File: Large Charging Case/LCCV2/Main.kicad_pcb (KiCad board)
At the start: 2 copper layers, 139.9 x 57.8 mm, 238 parts, among them J1 Conn_02x05_Odd_Even, J10 Coil A, J11 Coil B, J12 TX_Coil, J13 Coil A, J14 Coil B, J15 TX_Coil, J16 Coil A, J17 Coil B, J18 TX_Coil, J19 Coil A, J2 Coil B, J20 Coil B, J21 TX_Coil, J22 Coil A, J23 USB_C_Receptacle_USB2.0, J24 Conn_01x02, J25 Coil B, J26 TX_Coil, J27 Coil A, J3 TX_Coil, J4 Coil A, J5 Coil B, J6 TX_Coil, J7 Coil A, J8 Coil B, J9 TX_Coil, SW1 SW_Push, U1 N52810_QFN32, U10 XKT001, U11 XKT335, U12 XKT001, U13 XKT335, U14 XKT001, U15 XKT335, U16 INA4180A4, U17 DG4051E, U18 INA4180A4, U19 74HCT259, U2 XKT001, U20 BQ24232H, U21 XL6007E1, U22 LN3406, U23 XKT001, U24 XKT335, U3 XKT335, U4 XKT001, U5 XKT335, U6 XKT001, U7 XKT335, U8 XKT001, U9 XKT335, Y1 32MHz 40ppm

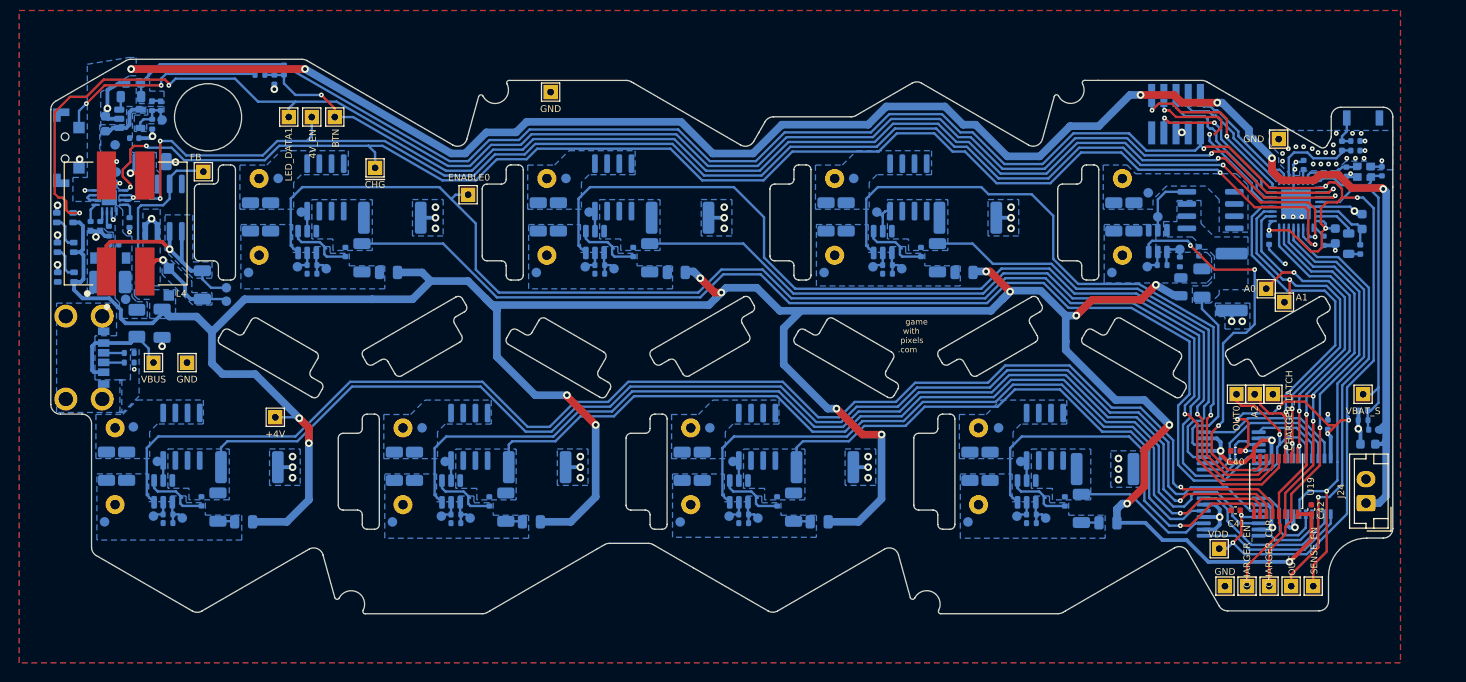
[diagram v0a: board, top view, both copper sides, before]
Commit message: Updating D8 and D10 boards, new antenna, etc...
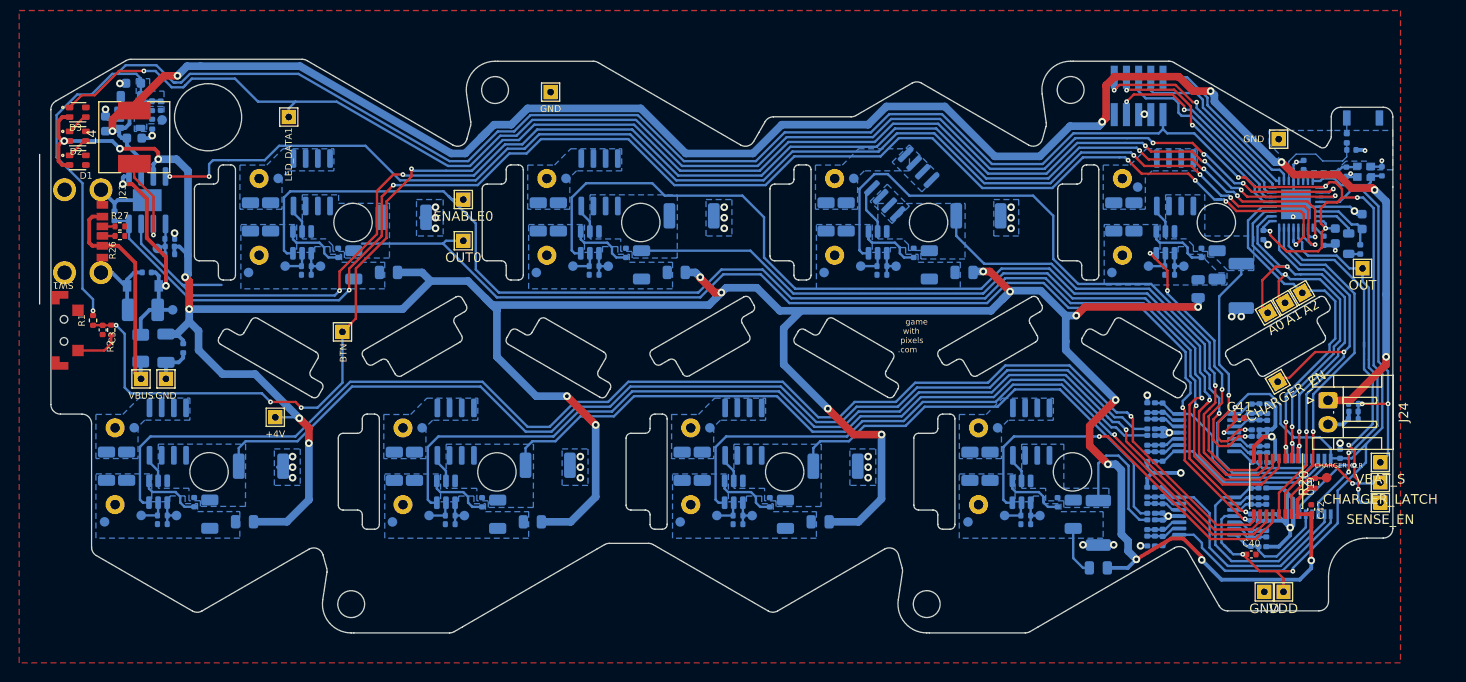
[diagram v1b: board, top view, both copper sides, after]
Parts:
- removed C9: DNP, Capacitor_SMD:C_0402_1005Metric
- removed D4: 30V 2A, Diode_SMD:D_SOD-123F
- removed U21: XL6007E1, Pixels-dice:SOIC-8_3.9x4.9mm_P1.27mm
- removed W11, W16, W21, W26, W31, W36, W6, W73: G, Pixels-dice:TEST_PIN
- removed W60: ~{PGOOD}, Pixels-dice:TEST_PIN
- removed W63: VDC, Pixels-dice:TEST_PIN
- removed W64: SWC, Pixels-dice:TEST_PIN
- removed W66: SW, Pixels-dice:TEST_PIN
- removed W78: ~{CHG}, Pixels-dice:TestPoint_THTPad_1.5x1.5mm_Drill0.7mm
- removed W79: 4V_EN, Pixels-dice:TestPoint_THTPad_1.5x1.5mm_Drill0.7mm
- added C59: 0.1uF 10V 20%, Capacitor_SMD:C_0402_1005Metric, B.Cu at (181.4, 109.3)
- added C60: 0.1uF 10V 20%, Capacitor_SMD:C_0402_1005Metric, B.Cu at (182.2, 111.0)
- added C61: 0.1uF 10V 20%, Capacitor_SMD:C_0402_1005Metric, B.Cu at (172.2, 114.3)
- added C62: 0.1uF 10V 20%, Capacitor_SMD:C_0402_1005Metric, B.Cu at (172.2, 112.6)
- added C63: 0.1uF 10V 20%, Capacitor_SMD:C_0402_1005Metric, B.Cu at (172.2, 109.2)
- added C64: 0.1uF 10V 20%, Capacitor_SMD:C_0402_1005Metric, B.Cu at (172.2, 110.9)
- added C65: 0.1uF 10V 20%, Capacitor_SMD:C_0402_1005Metric, B.Cu at (181.5, 100.5)
- added C66: 0.1uF 10V 20%, Capacitor_SMD:C_0402_1005Metric, B.Cu at (183.1, 102.2)
- added C67: 0.1uF 10V 20%, Capacitor_SMD:C_0402_1005Metric, B.Cu at (181.5, 105.6)
- added C68: 0.1uF 10V 20%, Capacitor_SMD:C_0402_1005Metric, B.Cu at (183.1, 103.9)
- added C69: 0.1uF 10V 20%, Capacitor_SMD:C_0402_1005Metric, B.Cu at (172.2, 105.5)
- added C70: 0.1uF 10V 20%, Capacitor_SMD:C_0402_1005Metric, B.Cu at (172.2, 103.8)
- added C71: 0.1uF 10V 20%, Capacitor_SMD:C_0402_1005Metric, B.Cu at (172.2, 100.4)
- added C72: 0.1uF 10V 20%, Capacitor_SMD:C_0402_1005Metric, B.Cu at (172.2, 102.1)
- added R39: 100k 0.1%, Resistor_SMD:R_0402_1005Metric, B.Cu at (171.4, 114.3)
- added R40: 2k 0.1%, Resistor_SMD:R_0402_1005Metric, B.Cu at (170.6, 114.3)
- added R41: 100mR 0.5W 1%, Resistor_SMD:R_2010_5025Metric, B.Cu at (165.5, 112.4)
- added R42: 2k 0.1%, Resistor_SMD:R_0402_1005Metric, B.Cu at (170.6, 112.6)
- added R43: 100k 0.1%, Resistor_SMD:R_0402_1005Metric, B.Cu at (171.4, 112.6)
- added R44: 100k 0.1%, Resistor_SMD:R_0402_1005Metric, B.Cu at (171.4, 109.2)
- added R45: 2k 0.1%, Resistor_SMD:R_0402_1005Metric, B.Cu at (170.6, 109.2)
- added R46: 100mR 0.5W 1%, Resistor_SMD:R_2010_5025Metric, B.Cu at (138.1, 106.5)
- added R47: 2k 0.1%, Resistor_SMD:R_0402_1005Metric, B.Cu at (170.6, 110.9)
- added R48: 100k 0.1%, Resistor_SMD:R_0402_1005Metric, B.Cu at (171.4, 110.9)
- added R49: 100k 0.1%, Resistor_SMD:R_0402_1005Metric, B.Cu at (182.3, 100.5)
- added R50: 2k 0.1%, Resistor_SMD:R_0402_1005Metric, B.Cu at (183.1, 100.5)
- added R51: 100mR 0.5W 1%, Resistor_SMD:R_2010_5025Metric, B.Cu at (180.4, 87.7)
- added R52: 2k 0.1%, Resistor_SMD:R_0402_1005Metric, B.Cu at (181.5, 102.2)
- added R53: 100k 0.1%, Resistor_SMD:R_0402_1005Metric, B.Cu at (182.3, 102.2)
- added R54: 100k 0.1%, Resistor_SMD:R_0402_1005Metric, B.Cu at (182.3, 105.6)
- added R55: 2k 0.1%, Resistor_SMD:R_0402_1005Metric, B.Cu at (183.1, 105.6)
- added R56: 100mR 0.5W 1%, Resistor_SMD:R_2010_5025Metric, B.Cu at (153.0, 80.4)
- added R57: 2k 0.1%, Resistor_SMD:R_0402_1005Metric, B.Cu at (181.5, 103.9)
- added R58: 100k 0.1%, Resistor_SMD:R_0402_1005Metric, B.Cu at (182.3, 103.9)
- added R59: 100k 0.1%, Resistor_SMD:R_0402_1005Metric, B.Cu at (171.4, 105.5)
- added R60: 2k 0.1%, Resistor_SMD:R_0402_1005Metric, B.Cu at (170.6, 105.5)
- added R61: 100mR 0.5W 1%, Resistor_SMD:R_2010_5025Metric, B.Cu at (108.1, 106.4)
- added R62: 2k 0.1%, Resistor_SMD:R_0402_1005Metric, B.Cu at (170.6, 103.8)
- added R63: 100k 0.1%, Resistor_SMD:R_0402_1005Metric, B.Cu at (171.4, 103.8)
- added R64: 100k 0.1%, Resistor_SMD:R_0402_1005Metric, B.Cu at (171.4, 100.4)
- added R65: 2k 0.1%, Resistor_SMD:R_0402_1005Metric, B.Cu at (170.6, 100.4)
- added R66: 100mR 0.5W 1%, Resistor_SMD:R_2010_5025Metric, B.Cu at (78.2, 106.5)
- added R67: 2k 0.1%, Resistor_SMD:R_0402_1005Metric, B.Cu at (170.6, 102.1)
- added R68: 100k 0.1%, Resistor_SMD:R_0402_1005Metric, B.Cu at (171.4, 102.1)
- C3, D1, D2, D3, J23, R1, R2, R26, R27, SW1: moved to F.Cu
- C45: value 0.1uF 10V 20% -> 4.7uF 6.3V 20%; footprint Capacitor_SMD:C_0402_1005Metric -> Capacitor_SMD:C_0603_1608Metric
- C46: value 47uF 10V 20% -> 22pF 10V 5%; footprint Capacitor_SMD:C_1206_3216Metric -> Capacitor_SMD:C_0402_1005Metric
- C49: value 4.7uF 6.3V 20% -> 0.1uF 10V 20%; footprint Capacitor_SMD:C_0603_1608Metric -> Capacitor_SMD:C_0402_1005Metric
- C5, C6: value 6pF 10V 10% -> 8pF 10V 10%
- C50: value 47uF 10V 20% -> 0.1uF 10V 20%; footprint Capacitor_SMD:C_1206_3216Metric -> Capacitor_SMD:C_0402_1005Metric
- C8: value 1.5pF 10V NP0 -> 0.8pF 10V NP0
- J24: footprint Connector_JST:JST_EH_B2B-EH-A_1x02_P2.50mm_Vertical -> Connector_JST:JST_EH_S2B-EH_1x02_P2.50mm_Horizontal
- L4: value 22uH 2A 20% -> 4.7uH 1.5A 10%; footprint Pixels-dice:Murata 4700 -> Pixels-dice:SPM6530
- R17: value 30mR 2W 1% -> 470k 1%; footprint Resistor_SMD:R_2512_6332Metric -> Resistor_SMD:R_0402_1005Metric
- R18: value 30mR 2W 1% -> 1k 1%; footprint Resistor_SMD:R_2512_6332Metric -> Resistor_SMD:R_0402_1005Metric
- R19: value 30mR 2W 1% -> 100k 1%; footprint Resistor_SMD:R_2512_6332Metric -> Resistor_SMD:R_0402_1005Metric
- R20: value 30mR 2W 1% -> 100k 1%; footprint Resistor_SMD:R_2512_6332Metric -> Resistor_SMD:R_0402_1005Metric; moved to F.Cu
- R21: value 30mR 2W 1% -> 100k 0.1%; footprint Resistor_SMD:R_2512_6332Metric -> Resistor_SMD:R_0402_1005Metric
- R22, R24: value 30mR 2W 1% -> 2k 0.1%; footprint Resistor_SMD:R_2512_6332Metric -> Resistor_SMD:R_0402_1005Metric
- R23: value 30mR 2W 1% -> 100mR 0.5W 1%; footprint Resistor_SMD:R_2512_6332Metric -> Resistor_SMD:R_2010_5025Metric
- R25: value 8.66k 1% -> 100k 0.1%
- R28: value 10k 5% -> 100k 0.1%
- R29: value 3k 1% -> 2k 0.1%
- R30: value 1k 1% -> 100mR 0.5W 1%; footprint Resistor_SMD:R_0402_1005Metric -> Resistor_SMD:R_2010_5025Metric
- R31: value 1.8k 1% -> 2k 0.1%
- R32: value 3.32k 1% -> 100k 0.1%
- U16: value INA4180A4 -> LP78071; footprint Package_SO:TSSOP-14_4.4x5mm_P0.65mm -> Pixels-dice:SOIC-8-1EP_3.9x4.9mm_P1.27mm_EP2.29x3mm
- U17: value DG4051E -> 74HC4051PW
- U18: value INA4180A4 -> LM2902
- U20: value BQ24232H -> LM2902; footprint Package_DFN_QFN:VQFN-16-1EP_3x3mm_P0.5mm_EP1.6x1.6mm -> Package_SO:TSSOP-14_4.4x5mm_P0.65mm
- W59: footprint Pixels-dice:TestPoint_THTPad_1.5x1.5mm_Drill0.7mm -> Pixels-dice:TEST_PIN
- W67: footprint Pixels-dice:TestPoint_THTPad_1.5x1.5mm_Drill0.7mm -> Pixels-dice:TEST_PIN; moved to B.Cu
- moved R28 124.9 mm to (182.2, 109.3)
- moved R29 123.7 mm to (183.0, 109.3)
- moved R31 123.5 mm to (181.4, 111.0), turned to 90 degrees
- moved R25 120.2 mm to (183.0, 112.7), turned to -90 degrees
- moved R32 119.6 mm to (183.0, 111.0), turned to 90 degrees
- moved U20 117.0 mm to (176.8, 103.0), turned to 180 degrees
- moved U16 116.0 mm to (66.3, 78.8), turned to 90 degrees
- moved C50 112.9 mm to (182.2, 112.7), turned to 90 degrees
- moved R24 104.6 mm to (181.4, 112.7), turned to -90 degrees
- moved R19 83.2 mm to (68.7, 82.8)
- moved W40 82.2 mm to (99.3, 83.0)
- moved R18 59.0 mm to (62.9, 80.4), turned to 90 degrees
- moved R30 58.6 mm to (123.1, 80.4), turned to 180 degrees
- moved R22 46.7 mm to (183.0, 114.4), turned to 90 degrees
- moved W47 33.9 mm to (193.0, 85.9)
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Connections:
- net Net-(AE1-Pad1) renamed /ANT_CHIP
- net Net-(C8-Pad2) renamed /ANT_NRF
- C45 pad 1: +VDC -> +BATT
- C46 pad 1: +VDC -> +4V
- C46 pad 2: GND -> Net-(C46-Pad2)
- C49 pad 1: +BATT -> Net-(C49-Pad1)
- C49 pad 2: GND -> /Multiplexed Chargers/SENSE5
- C50 pad 2: Net-(C50-Pad2) -> GND
- C53 pad 1: +VDC -> +BATT
- L4 pad 1: Net-(C50-Pad1) -> Net-(L4-Pad1)
- L4 pad 2: Net-(C50-Pad2) -> +BATT
- R17 pad 1: GND -> Net-(C46-Pad2)
- R17 pad 2: /Multiplexed Chargers/Charger 1/CHARGER_GND -> +4V
- R18 pad 1: GND -> /Power/BAT_I_SENSE
- R18 pad 2: /Multiplexed Chargers/Charger 2/CHARGER_GND -> GND
- R19 pad 2: /Multiplexed Chargers/Charger 3/CHARGER_GND -> Net-(C46-Pad2)
- R20 pad 1: GND -> +4V
- R20 pad 2: /Multiplexed Chargers/Charger 4/CHARGER_GND -> Net-(R20-Pad2)
- R21 pad 1: GND -> /Multiplexed Chargers/SENSE5
- R21 pad 2: /Multiplexed Chargers/Charger 5/CHARGER_GND -> Net-(C49-Pad1)
- R22 pad 2: /Multiplexed Chargers/Charger 6/CHARGER_GND -> Net-(C49-Pad1)
- R23 pad 2: /Multiplexed Chargers/Charger 7/CHARGER_GND -> /Multiplexed Chargers/Charger 1/CHARGER_GND
- R24 pad 1: GND -> /Multiplexed Chargers/Charger 1/CHARGER_GND
- R24 pad 2: /Multiplexed Chargers/Charger 8/CHARGER_GND -> Net-(C50-Pad1)
- R25 pad 1: +4V -> GND
- R25 pad 2: Net-(R25-Pad2) -> Net-(C50-Pad1)
- R28 pad 1: Net-(R28-Pad1) -> /Multiplexed Chargers/SENSE7
- R28 pad 2: GND -> Net-(C59-Pad1)
- R29 pad 1: Net-(R29-Pad1) -> GND
- R29 pad 2: GND -> Net-(C59-Pad1)
- R30 pad 1: Net-(R30-Pad1) -> GND
- R30 pad 2: GND -> /Multiplexed Chargers/Charger 2/CHARGER_GND
- R31 pad 1: Net-(R31-Pad1) -> /Multiplexed Chargers/Charger 2/CHARGER_GND
- R31 pad 2: GND -> Net-(C60-Pad1)
- R32 pad 1: Net-(R25-Pad2) -> GND
- R32 pad 2: GND -> Net-(C60-Pad1)
- U1 pad 2: /Power/4V_EN -> /Power/CHARGE
- U1 pad 3: /Power/~{CHG} -> /Power/4V_EN
- U1 pad 5: /Multiplexed Chargers/SENSE_EN -> /Power/BAT_I_SENSE
- U1 pad 6: /Multiplexed Chargers/~{CHARGER_ENL_CLR} -> /Multiplexed Chargers/SENSE_EN
- U10 pad 6: /Multiplexed Chargers/ENABLE5 -> /Multiplexed Chargers/ENABLE6
- U12 pad 6: /Multiplexed Chargers/ENABLE6 -> /Multiplexed Chargers/ENABLE5
- U14 pad 6: /Multiplexed Chargers/ENABLE7 -> /Multiplexed Chargers/ENABLE4
- U16 pad 1: /Multiplexed Chargers/SENSE0 -> Net-(C46-Pad2)
- U16 pad 2: GND -> Net-(L4-Pad1)
- U16 pad 3: /Multiplexed Chargers/Charger 2/CHARGER_GND -> /Power/CHARGE
- U16 pad 4: VDD -> /Power/BAT_I_SENSE
- U16 pad 5: /Multiplexed Chargers/Charger 1/CHARGER_GND -> +5V
- U16 pad 6: GND -> +BATT
- U16 pad 7: /Multiplexed Chargers/SENSE3 -> +4V
- U16 pad 8: /Multiplexed Chargers/SENSE1 -> /Power/4V_EN
- U18 pad 1: /Multiplexed Chargers/SENSE5 -> /Multiplexed Chargers/SENSE7
- U18 pad 10: /Multiplexed Chargers/Charger 5/CHARGER_GND -> Net-(C62-Pad1)
- U18 pad 12: /Multiplexed Chargers/Charger 6/CHARGER_GND -> Net-(C64-Pad1)
- U18 pad 13: GND -> Net-(C63-Pad1)
- U18 pad 2: GND -> Net-(C59-Pad1)
- U18 pad 3: /Multiplexed Chargers/Charger 8/CHARGER_GND -> Net-(C60-Pad1)
- U18 pad 5: /Multiplexed Chargers/Charger 7/CHARGER_GND -> Net-(C50-Pad1)
- U18 pad 6: GND -> Net-(C49-Pad1)
- U18 pad 7: /Multiplexed Chargers/SENSE7 -> /Multiplexed Chargers/SENSE5
- U18 pad 9: GND -> Net-(C61-Pad1)
- U19 pad 15: /Multiplexed Chargers/~{CHARGER_ENL_CLR} -> Net-(R20-Pad2)
- U20 pad 1: Net-(R28-Pad1) -> /Multiplexed Chargers/SENSE0
- U20 pad 10: +VDC -> Net-(C70-Pad1)
- U20 pad 11: +VDC -> GND
- U20 pad 12: Net-(R30-Pad1) -> Net-(C72-Pad1)
- U20 pad 13: +5V -> Net-(C71-Pad1)
- U20 pad 14: GND -> /Multiplexed Chargers/SENSE1
- U20 pad 2: +BATT -> Net-(C65-Pad1)
- U20 pad 3: +BATT -> Net-(C66-Pad1)
- U20 pad 4: GND -> VDD
- U20 pad 5: +VDC -> Net-(C68-Pad1)
- U20 pad 6: GND -> Net-(C67-Pad1)
- U20 pad 7: Net-(U20-Pad7) -> /Multiplexed Chargers/SENSE3
- U20 pad 8: GND -> /Multiplexed Chargers/SENSE2
- U20 pad 9: /Power/~{CHG} -> Net-(C69-Pad1)
- U22 pad 1: +VDC -> +BATT
- U22 pad 4: +VDC -> +BATT
- U23 pad 6: /Multiplexed Chargers/ENABLE4 -> /Multiplexed Chargers/ENABLE7
- W40 pad 1: /Multiplexed Chargers/SENSE3 -> /Multiplexed Chargers/Charger 1/CHARGER_GND
- W59 pad 1: /Multiplexed Chargers/~{CHARGER_ENL_CLR} -> Net-(R20-Pad2)
- W67 pad 1: Net-(R25-Pad2) -> Net-(C46-Pad2)
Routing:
- net /Power/CHARGE: track 0.00 -> 156.5 mm, vias 0 -> 6
- net /Power/BAT_I_SENSE: track 0.00 -> 154.7 mm, vias 0 -> 6
- net /Power/~{CHG}: track 150.5 -> 0.00 mm, vias 4 -> 0
- net /Multiplexed Chargers/ENABLE7: track 143.5 -> 41.1 mm
- net /Multiplexed Chargers/ENABLE4: track 40.7 -> 142.3 mm
- net /Multiplexed Chargers/~{CHARGER_ENL_CLR}: track 45.6 -> 0.00 mm, vias 1 -> 0
- net Net-(C3-Pad1): track 128.5 -> 169.2 mm, vias 3 -> 8
- net VDD: track 249.1 -> 288.5 mm, vias 12 -> 10
- net /Multiplexed Chargers/ENABLE6: track 108.9 -> 74.6 mm
- net /Multiplexed Chargers/ENABLE5: track 75.1 -> 108.0 mm
- net +4V: track 311.9 -> 342.8 mm, vias 15 -> 22
- net +5V: track 0.00 -> 25.1 mm, vias 0 -> 2
- net /Multiplexed Chargers/Charger 7/CHARGER_GND: track 97.4 -> 75.0 mm
- net /Multiplexed Chargers/Charger 8/CHARGER_GND: track 129.9 -> 109.4 mm
- net Net-(C50-Pad1): track 23.2 -> 3.71 mm, vias 1 -> 0
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- removed copper zone on B.Cu, net +4V
- removed copper zone on B.Cu, net +5V
- removed copper zone on B.Cu, net +BATT
- removed copper zone on B.Cu, net +VDC
- removed copper zone on B.Cu, net Net-(C50-Pad1)
- removed copper zone on B.Cu, net Net-(C50-Pad2)
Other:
- board size 139.9 x 57.8 mm -> 139.9 x 59.8 mm

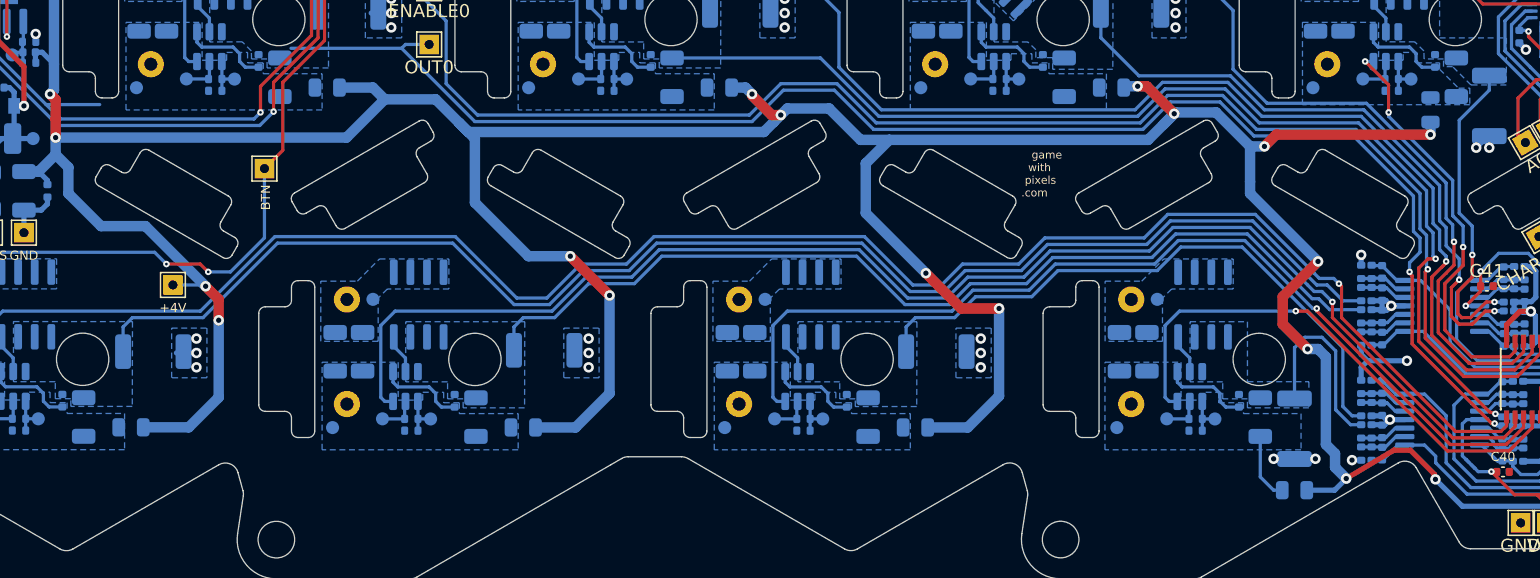
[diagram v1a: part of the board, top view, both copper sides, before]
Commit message: D20V13 and D20V13 RF Testboard 1. Also tweaks to LCCV2
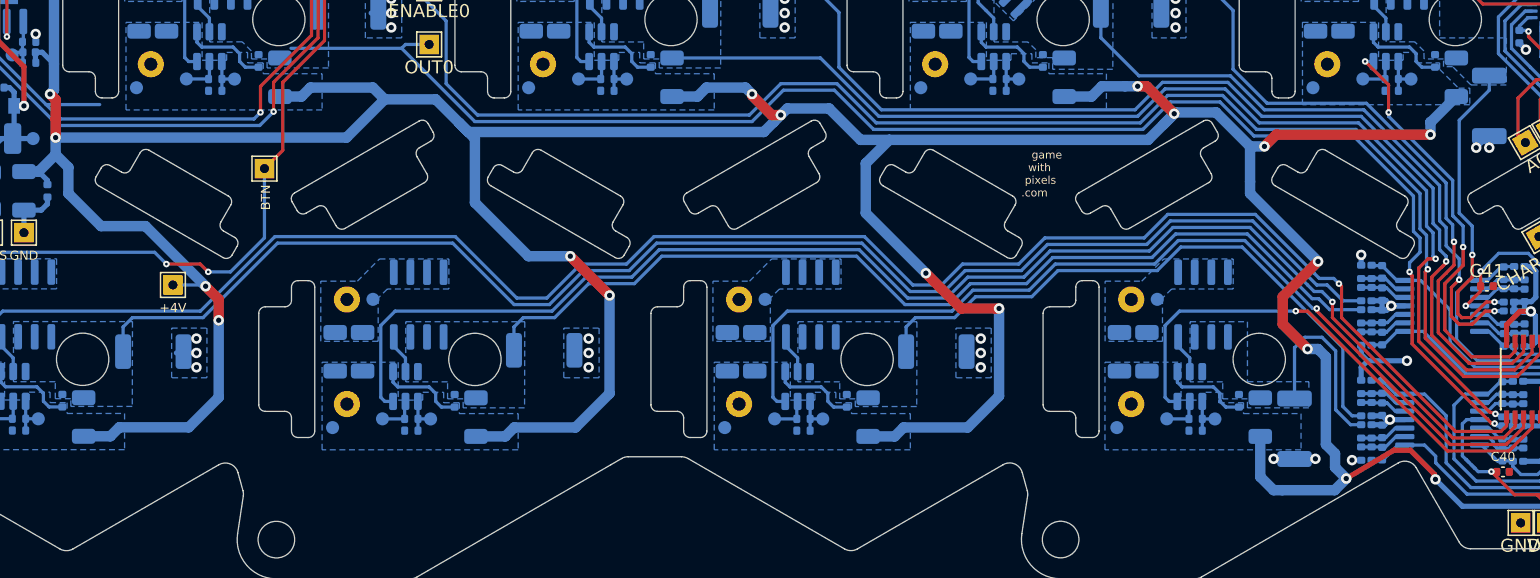
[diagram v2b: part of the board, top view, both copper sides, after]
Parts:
- removed F2, F3, F4, F5, F6, F7, F8, F9: 500mA ~150mR, Fuse:Fuse_0805_2012Metric
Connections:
- C11 pad 1: Net-(C11-Pad1) -> +4V
- C12 pad 1: Net-(C11-Pad1) -> +4V
- C13 pad 2: Net-(C11-Pad1) -> +4V
- C14 pad 2: Net-(C11-Pad1) -> +4V
- C15 pad 1: Net-(C15-Pad1) -> +4V
- C16 pad 1: Net-(C15-Pad1) -> +4V
- C17 pad 2: Net-(C15-Pad1) -> +4V
- C18 pad 2: Net-(C15-Pad1) -> +4V
- C19 pad 1: Net-(C19-Pad1) -> +4V
- C20 pad 1: Net-(C19-Pad1) -> +4V
- C21 pad 2: Net-(C19-Pad1) -> +4V
- C22 pad 2: Net-(C19-Pad1) -> +4V
- C23 pad 1: Net-(C23-Pad1) -> +4V
- C24 pad 1: Net-(C23-Pad1) -> +4V
- C25 pad 2: Net-(C23-Pad1) -> +4V
- C26 pad 2: Net-(C23-Pad1) -> +4V
- C27 pad 1: Net-(C27-Pad1) -> +4V
- C28 pad 1: Net-(C27-Pad1) -> +4V
- C29 pad 2: Net-(C27-Pad1) -> +4V
- C30 pad 2: Net-(C27-Pad1) -> +4V
- C31 pad 1: Net-(C31-Pad1) -> +4V
- C32 pad 1: Net-(C31-Pad1) -> +4V
- C33 pad 2: Net-(C31-Pad1) -> +4V
- C34 pad 2: Net-(C31-Pad1) -> +4V
- C35 pad 1: Net-(C35-Pad1) -> +4V
- C36 pad 1: Net-(C35-Pad1) -> +4V
- C37 pad 2: Net-(C35-Pad1) -> +4V
- C38 pad 2: Net-(C35-Pad1) -> +4V
- C49 pad 2: /Multiplexed Chargers/SENSE5 -> /Multiplexed Chargers/SENSE0
- C55 pad 1: Net-(C55-Pad1) -> +4V
- C56 pad 1: Net-(C55-Pad1) -> +4V
- C57 pad 2: Net-(C55-Pad1) -> +4V
- C58 pad 2: Net-(C55-Pad1) -> +4V
- C59 pad 2: /Multiplexed Chargers/SENSE7 -> /Multiplexed Chargers/SENSE1
- C63 pad 2: /Multiplexed Chargers/SENSE6 -> /Multiplexed Chargers/SENSE5
- C65 pad 2: /Multiplexed Chargers/SENSE0 -> /Multiplexed Chargers/SENSE3
- C67 pad 2: /Multiplexed Chargers/SENSE3 -> /Multiplexed Chargers/SENSE2
- C69 pad 2: /Multiplexed Chargers/SENSE2 -> /Multiplexed Chargers/SENSE6
- C71 pad 2: /Multiplexed Chargers/SENSE1 -> /Multiplexed Chargers/SENSE7
- J11 pad 1: Net-(C23-Pad1) -> +4V
- J14 pad 1: Net-(C27-Pad1) -> +4V
- J17 pad 1: Net-(C31-Pad1) -> +4V
- J2 pad 1: Net-(C11-Pad1) -> +4V
- J20 pad 1: Net-(C35-Pad1) -> +4V
- J25 pad 1: Net-(C55-Pad1) -> +4V
- J5 pad 1: Net-(C15-Pad1) -> +4V
- J8 pad 1: Net-(C19-Pad1) -> +4V
- R11 pad 2: Net-(C27-Pad1) -> +4V
- R13 pad 2: Net-(C31-Pad1) -> +4V
- R15 pad 2: Net-(C35-Pad1) -> +4V
- R21 pad 1: /Multiplexed Chargers/SENSE5 -> /Multiplexed Chargers/SENSE0
- R28 pad 1: /Multiplexed Chargers/SENSE7 -> /Multiplexed Chargers/SENSE1
- R3 pad 2: Net-(C11-Pad1) -> +4V
- R37 pad 2: Net-(C55-Pad1) -> +4V
- R44 pad 1: /Multiplexed Chargers/SENSE6 -> /Multiplexed Chargers/SENSE5
- R49 pad 1: /Multiplexed Chargers/SENSE0 -> /Multiplexed Chargers/SENSE3
- R5 pad 2: Net-(C15-Pad1) -> +4V
- R54 pad 1: /Multiplexed Chargers/SENSE3 -> /Multiplexed Chargers/SENSE2
- R59 pad 1: /Multiplexed Chargers/SENSE2 -> /Multiplexed Chargers/SENSE6
- R64 pad 1: /Multiplexed Chargers/SENSE1 -> /Multiplexed Chargers/SENSE7
- R7 pad 2: Net-(C19-Pad1) -> +4V
- R9 pad 2: Net-(C23-Pad1) -> +4V
- U10 pad 1: Net-(C27-Pad1) -> +4V
- U12 pad 1: Net-(C31-Pad1) -> +4V
- U14 pad 1: Net-(C35-Pad1) -> +4V
- U17 pad 12: /Multiplexed Chargers/SENSE3 -> /Multiplexed Chargers/SENSE2
- U17 pad 13: /Multiplexed Chargers/SENSE0 -> /Multiplexed Chargers/SENSE3
- U17 pad 14: /Multiplexed Chargers/SENSE1 -> /Multiplexed Chargers/SENSE7
- U17 pad 15: /Multiplexed Chargers/SENSE2 -> /Multiplexed Chargers/SENSE6
- U17 pad 2: /Multiplexed Chargers/SENSE6 -> /Multiplexed Chargers/SENSE5
- U17 pad 4: /Multiplexed Chargers/SENSE7 -> /Multiplexed Chargers/SENSE1
- U17 pad 5: /Multiplexed Chargers/SENSE5 -> /Multiplexed Chargers/SENSE0
- U18 pad 1: /Multiplexed Chargers/SENSE7 -> /Multiplexed Chargers/SENSE1
- U18 pad 14: /Multiplexed Chargers/SENSE6 -> /Multiplexed Chargers/SENSE5
- U18 pad 7: /Multiplexed Chargers/SENSE5 -> /Multiplexed Chargers/SENSE0
- U2 pad 1: Net-(C11-Pad1) -> +4V
- U20 pad 1: /Multiplexed Chargers/SENSE0 -> /Multiplexed Chargers/SENSE3
- U20 pad 14: /Multiplexed Chargers/SENSE1 -> /Multiplexed Chargers/SENSE7
- U20 pad 7: /Multiplexed Chargers/SENSE3 -> /Multiplexed Chargers/SENSE2
- U20 pad 8: /Multiplexed Chargers/SENSE2 -> /Multiplexed Chargers/SENSE6
- U23 pad 1: Net-(C55-Pad1) -> +4V
- U4 pad 1: Net-(C15-Pad1) -> +4V
- U6 pad 1: Net-(C19-Pad1) -> +4V
- U8 pad 1: Net-(C23-Pad1) -> +4V
- W14 pad 1: Net-(C19-Pad1) -> +4V
- W19 pad 1: Net-(C23-Pad1) -> +4V
- W24 pad 1: Net-(C27-Pad1) -> +4V
- W29 pad 1: Net-(C31-Pad1) -> +4V
- W34 pad 1: Net-(C35-Pad1) -> +4V
- W4 pad 1: Net-(C11-Pad1) -> +4V
- W71 pad 1: Net-(C55-Pad1) -> +4V
- W9 pad 1: Net-(C15-Pad1) -> +4V
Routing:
- net +4V: track 342.8 -> 434.9 mm
- net /Multiplexed Chargers/SENSE5: track 11.3 -> 25.9 mm
- net Net-(C55-Pad1): track 11.9 -> 0.00 mm
- net /Multiplexed Chargers/SENSE2: track 20.9 -> 9.17 mm
- net /Multiplexed Chargers/SENSE3: track 9.17 -> 20.6 mm
- net /Multiplexed Chargers/SENSE0: track 20.6 -> 11.3 mm
- net Net-(C35-Pad1): track 6.66 -> 0.00 mm
- net Net-(C19-Pad1): track 6.66 -> 0.00 mm
- net Net-(C15-Pad1): track 6.66 -> 0.00 mm
- net Net-(C23-Pad1): track 6.66 -> 0.00 mm
- net Net-(C11-Pad1): track 6.66 -> 0.00 mm
- net Net-(C31-Pad1): track 6.66 -> 0.00 mm
- net Net-(C27-Pad1): track 6.66 -> 0.00 mm
- net /Multiplexed Chargers/SENSE6: track 25.9 -> 20.9 mm
- added copper zone on B.Cu, net +4V
- removed copper zone on B.Cu, net Net-(C11-Pad1)
- removed copper zone on B.Cu, net Net-(C15-Pad1)
- removed copper zone on B.Cu, net Net-(C19-Pad1)
- removed copper zone on B.Cu, net Net-(C23-Pad1)
- removed copper zone on B.Cu, net Net-(C27-Pad1)
- removed copper zone on B.Cu, net Net-(C31-Pad1)
- removed copper zone on B.Cu, net Net-(C35-Pad1)
- removed copper zone on B.Cu, net Net-(C55-Pad1)

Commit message: Large Charging Case V2 Outline and Keepout zones.
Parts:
- moved AE1 281.6 mm to (473.0, 72.6)
- moved C1 281.6 mm to (474.6, 83.4)
- moved C10 281.6 mm to (464.3, 84.8)
- moved C11 281.6 mm to (397.8, 86.7)
- moved C12 281.6 mm to (399.5, 87.9)
- moved C14 281.6 mm to (390.8, 82.9)
- moved C15 281.6 mm to (427.8, 86.7)
- moved C16 281.6 mm to (429.5, 87.9)
- moved C18 281.6 mm to (420.8, 82.9)
- moved C19 281.6 mm to (457.8, 86.7)
- moved C2 281.6 mm to (471.8, 84.9)
- moved C20 281.6 mm to (459.5, 87.9)
- moved C22 281.6 mm to (450.8, 82.9)
- moved C23 281.6 mm to (367.8, 86.7)
- moved C24 281.6 mm to (369.5, 87.9)
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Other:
- board size 139.9 x 59.8 mm -> 398.5 x 59.8 mm

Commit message: Commiting WangQing's new layout.
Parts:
- added P1: heard4, Pixels-dice:4x2.54mm_SMD, B.Cu at (130.7, 66.2)
- C3, C40, C41, C42, D1, D2, D3, J23, L4, R1, R2, R20, R26, R27, SW1, U19, W59: moved to B.Cu
- moved W3 316.6 mm to (147.9, 114.7)
- moved J1 297.5 mm to (153.8, 66.1)
- moved W2 282.7 mm to (107.3, 66.0)
- moved W1 281.6 mm to (81.3, 62.1)
- moved W41 279.8 mm to (189.7, 116.4)
- moved C39 278.8 mm to (193.5, 109.0), turned to 0 degrees
- moved W42 275.9 mm to (191.7, 115.2)
- moved W59 275.2 mm to (195.7, 113.6), turned to 180 degrees
- moved W68 275.1 mm to (195.7, 73.0)
- moved R20 274.1 mm to (195.7, 115.5)
- moved C42 273.6 mm to (195.7, 117.4), turned to -90 degrees
- moved W43 271.9 mm to (193.6, 114.1)
- moved W58 271.5 mm to (205.2, 119.5)
- moved C40 271.1 mm to (192.8, 96.0)
- moved W76 269.6 mm to (98.7, 94.0)
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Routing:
- net +4V: track 434.9 -> 355.5 mm, vias 22 -> 6
- net SWDIO: track 18.0 -> 95.8 mm, vias 0 -> 4
- net SWDCLK: track 19.1 -> 95.0 mm, vias 0 -> 4
- net RESET: track 23.1 -> 64.8 mm, vias 2 -> 4
- net RXI: track 21.8 -> 62.4 mm
- net SWO: track 21.0 -> 59.0 mm, vias 0 -> 4
- net TXO: track 22.9 -> 60.4 mm, vias 2 -> 4
- net /Multiplexed Chargers/CHARGER_SELECT_A2: track 37.1 -> 70.5 mm, vias 2 -> 6
- net VDD: track 288.5 -> 260.8 mm, vias 10 -> 9
- net /Multiplexed Chargers/CHARGER_SELECT_A1: track 40.2 -> 67.6 mm, vias 3 -> 6
- net /Multiplexed Chargers/CHARGER_SELECT_A0: track 42.2 -> 64.0 mm, vias 3 -> 6
- net /Multiplexed Chargers/~{CHARGER_ENL_EN}: track 45.3 -> 65.4 mm
- net /Power/VBAT_SENSE: track 39.8 -> 19.6 mm, vias 2 -> 0
- net +BATT: track 197.7 -> 181.0 mm, vias 7 -> 6
- net /Power/4V_EN: track 141.3 -> 155.1 mm, vias 6 -> 4
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- added copper zone on B.Cu, net +5V
- removed copper zone on B.Cu, net Net-(C51-Pad2)
- removed copper zone on B.Cu, net VDD
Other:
- board size 398.5 x 59.8 mm -> 136.2 x 62.1 mm
